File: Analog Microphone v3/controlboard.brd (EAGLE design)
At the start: 66 x 68.2 mm, 30 parts, among them J2 USB_A_SMT_FEMALE, Q1 12MHz

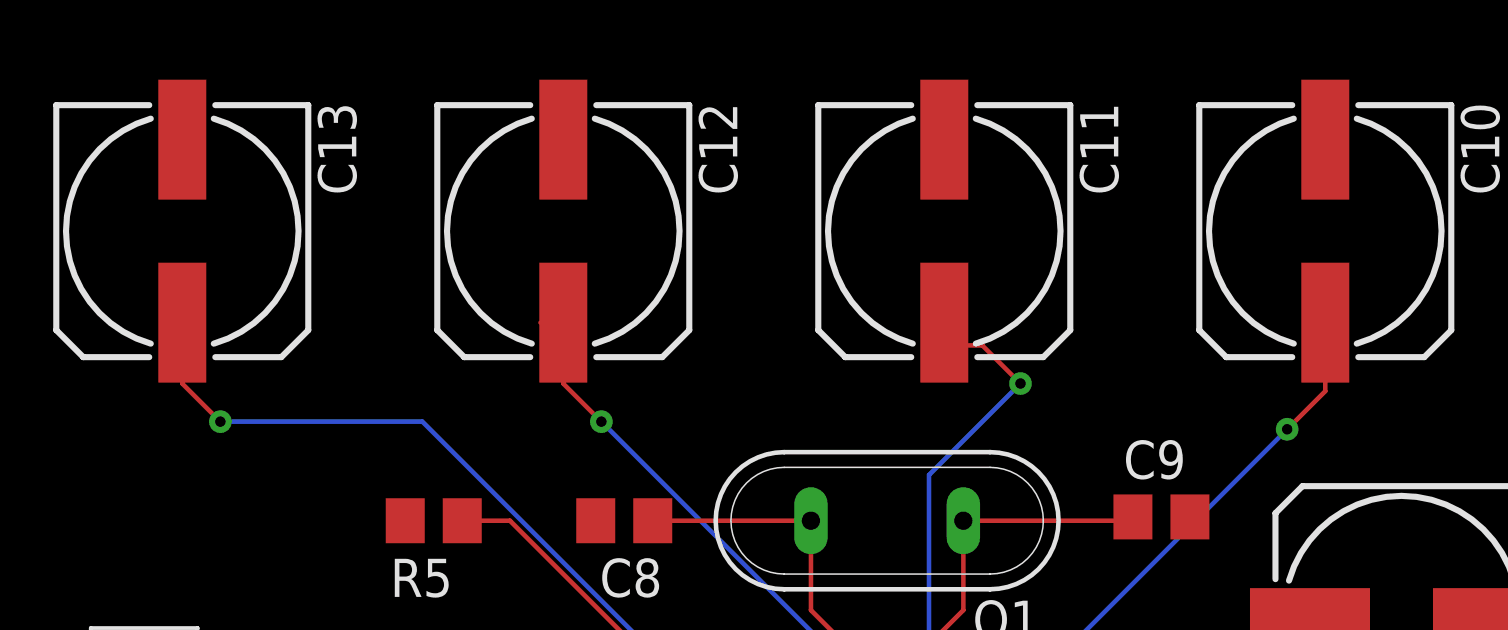
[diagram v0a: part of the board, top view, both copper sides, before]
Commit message: Update Analog Microphone v3/controlboard.brd
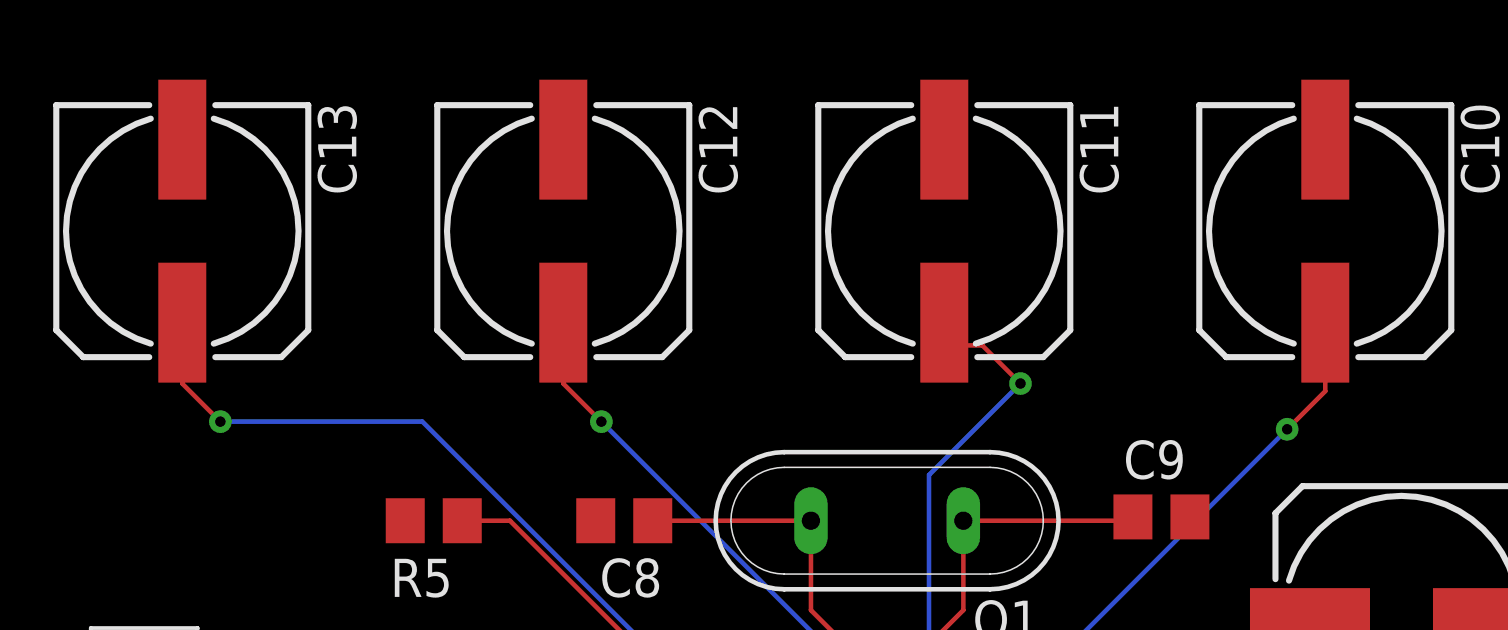
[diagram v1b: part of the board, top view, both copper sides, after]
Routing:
- net N$8: track 20.7 -> 20.0 mm
- net N$7: track 21.8 -> 21.3 mm
- net N$4: track 19.9 -> 19.4 mm
- net N$11: track 56.6 -> 56.1 mm
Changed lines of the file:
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@@
 <wire x1="35.9156" y1="42.2656" x2="36.322" y2="42.672" width="0.1524" layer="1"/>
 <via x="36.322" y="42.672" extent="1-16" drill="0.35"/>
-<wire x1="36.83" y1="57.15" x2="36.83" y2="56.64" width="0.1524" layer="1"/>
 <wire x1="36.322" y1="42.672" x2="36.322" y2="51.562" width="0.1524" layer="16"/>
 <wire x1="36.322" y1="51.562" x2="39.37" y2="54.61" width="0.1524" layer="16"/>
@@
 <via x="37.846" y="42.672" extent="1-16" drill="0.35"/>
 <wire x1="37.846" y1="42.672" x2="48.26" y2="53.086" width="0.1524" layer="16"/>
-<wire x1="49.53" y1="57.15" x2="49.53" y2="56.64" width="0.1524" layer="1"/>
 <via x="48.26" y="53.086" extent="1-16" drill="0.35"/>
 <wire x1="48.26" y1="53.086" x2="49.53" y2="54.356" width="0.1524" layer="1"/>
@@
 <via x="32.639" y="43.561" extent="1-16" drill="0.35"/>
 <wire x1="32.639" y1="43.561" x2="32.639" y2="46.101" width="0.1524" layer="16"/>
-<wire x1="24.13" y1="56.64" x2="23.37" y2="56.64" width="0.1524" layer="1"/>
 <wire x1="32.639" y1="46.101" x2="25.4" y2="53.34" width="0.1524" layer="16"/>
 <via x="25.4" y="53.34" extent="1-16" drill="0.35"/>
@@
 <wire x1="30.7086" y1="42.0624" x2="29.972" y2="42.799" width="0.1524" layer="1"/>
 <via x="29.972" y="42.799" extent="1-16" drill="0.35"/>
-<wire x1="11.43" y1="57.15" x2="11.43" y2="56.64" width="0.1524" layer="1"/>
 <wire x1="29.972" y1="42.799" x2="19.431" y2="53.34" width="0.1524" layer="16"/>
 <wire x1="19.431" y1="53.34" x2="12.7" y2="53.34" width="0.1524" layer="16"/>

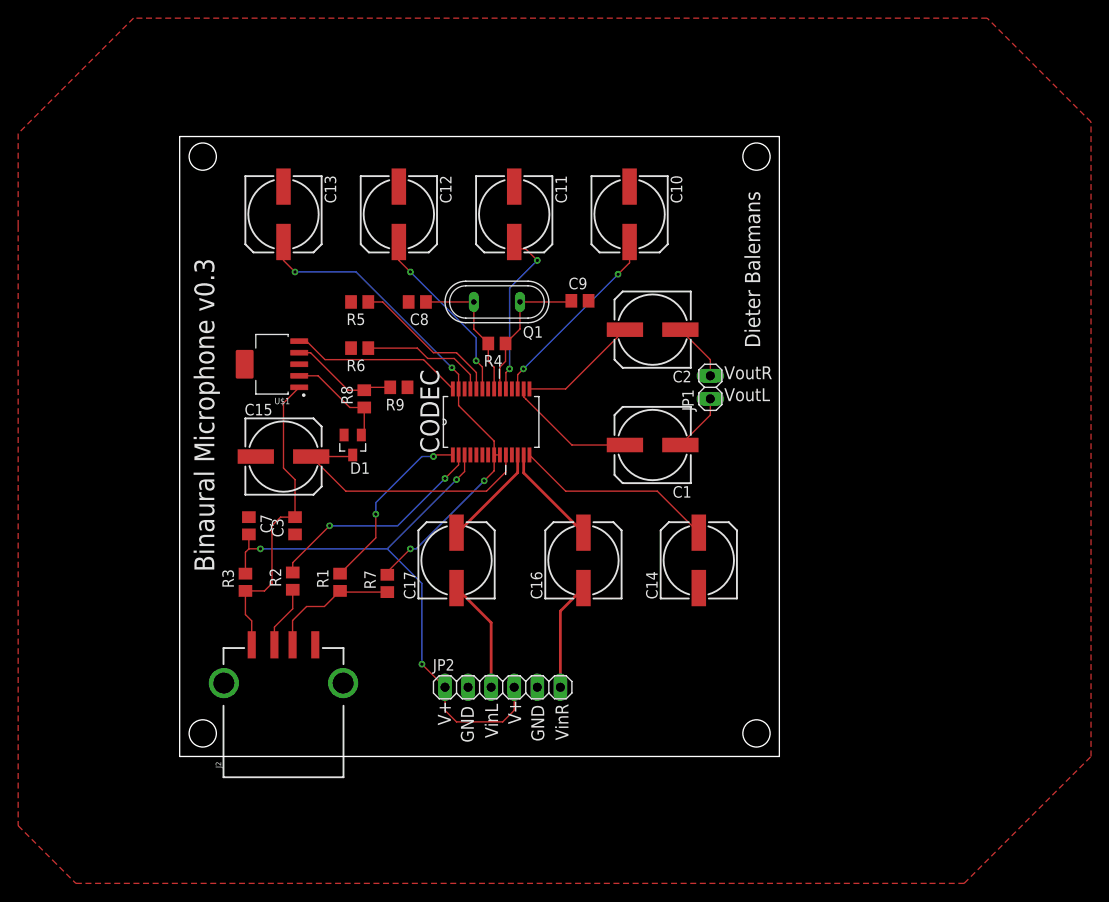
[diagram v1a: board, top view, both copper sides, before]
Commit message: Added bottom ground plane + usb test headers
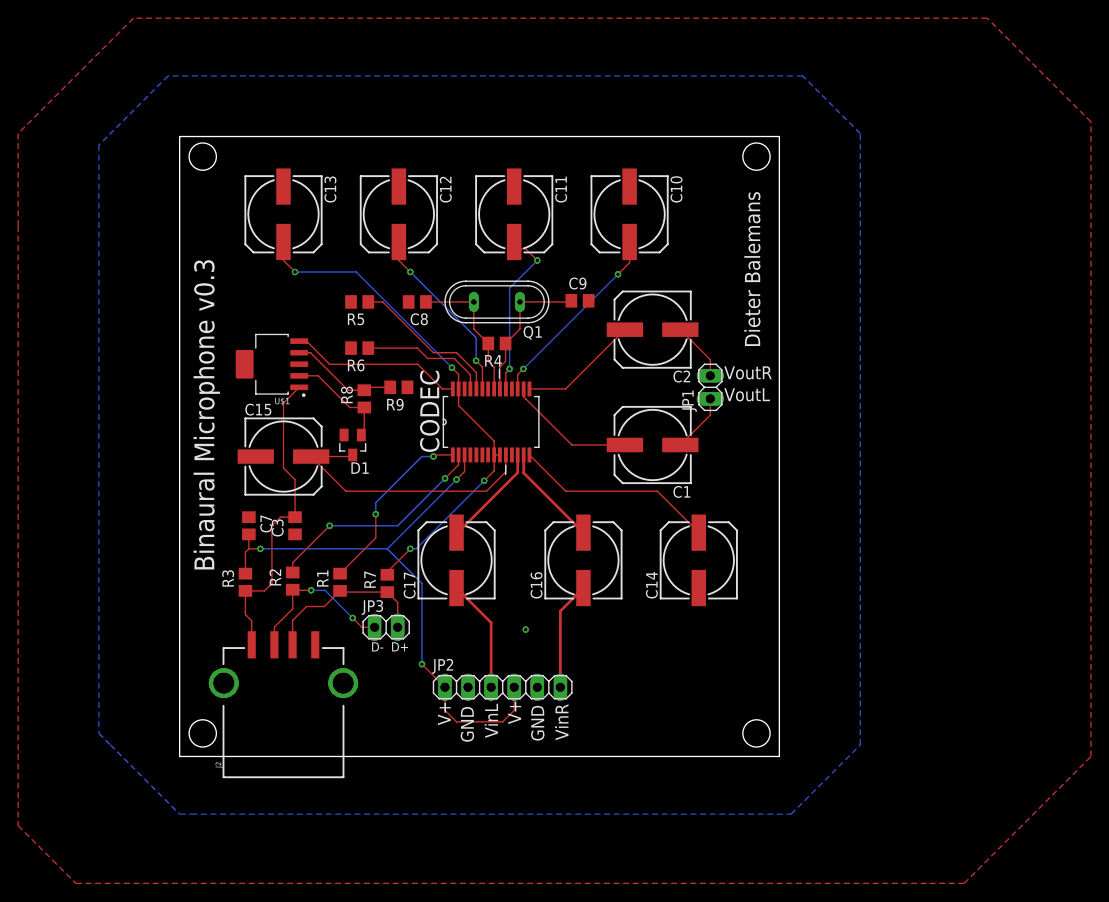
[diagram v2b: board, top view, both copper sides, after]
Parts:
- added JP3: (no value), pinhead:1X02
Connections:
- net D+: now also JP3.2
- net D-: now also JP3.1
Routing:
- net D-: track 6.90 -> 17.6 mm, vias 0 -> 2
- net D+: track 14.6 -> 18.9 mm
- added copper zone on layer 16, net GND
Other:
- board text added: "D+"
- board text added: "D-"
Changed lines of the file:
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@@
 <text x="59.944" y="41.529" size="1.4224" layer="25">VoutR</text>
 <text x="59.944" y="39.116" size="1.4224" layer="25">VoutL</text>
+<text x="25.273" y="12.573" size="1.016" layer="25" rot="R180">D+</text>
+<text x="22.479" y="12.573" size="1.016" layer="25" rot="R180">D-</text>
 </plain>
 <attributes>
@@
 <attribute name="VALUE" x="12.16" y="47.68" size="0.7" layer="27" rot="R180"/>
 </element>
+<element name="JP3" library="pinhead" library_urn="urn:adsk.eagle:library:325" package="1X02" package3d_urn="urn:adsk.eagle:package:22435/2" value="" x="22.733" y="14.224" smashed="yes">
+<attribute name="NAME" x="20.1168" y="15.9258" size="1.27" layer="25" ratio="10"/>
+<attribute name="VALUE" x="20.193" y="11.049" size="1.27" layer="27"/>
+</element>
 </elements>
 <signals>
@@
 <wire x1="12.43" y1="14.97" x2="12.43" y2="12.292" width="0.1524" layer="1"/>
 <wire x1="22.86" y1="18.1" x2="17.526" y2="18.1" width="0.1524" layer="1"/>
+<contactref element="JP3" pad="2"/>
+<wire x1="24.003" y1="14.224" x2="24.003" y2="16.957" width="0.1524" layer="1"/>
+<wire x1="24.003" y1="16.957" x2="22.86" y2="18.1" width="0.1524" layer="1"/>
 </signal>
 <signal name="D-">
@@
 <wire x1="10.43" y1="14.24" x2="10.43" y2="12.292" width="0.1524" layer="1"/>
 <wire x1="12.446" y1="16.256" x2="10.43" y2="14.24" width="0.1524" layer="1"/>
+<contactref element="JP3" pad="1"/>
+<wire x1="21.463" y1="14.224" x2="20.066" y2="14.224" width="0.1524" layer="1"/>
+<wire x1="20.066" y1="14.224" x2="19.05" y2="15.24" width="0.1524" layer="1"/>
+<via x="19.05" y="15.24" extent="1-16" drill="0.35"/>
+<wire x1="19.05" y1="15.24" x2="16.002" y2="18.288" width="0.1524" layer="16"/>
+<wire x1="16.002" y1="18.288" x2="14.478" y2="18.288" width="0.1524" layer="16"/>
+<via x="14.478" y="18.288" extent="1-16" drill="0.35"/>
+<wire x1="14.478" y1="18.288" x2="12.512" y2="18.288" width="0.1524" layer="1"/>
+<wire x1="12.512" y1="18.288" x2="12.446" y2="18.354" width="0.1524" layer="1"/>
 </signal>
 <signal name="GND">
@@
 <vertex x="-17.78" y="68.58"/>
 </polygon>
+<polygon width="0.1524" layer="16">
+<vertex x="-7.62" y="1.27"/>
+<vertex x="0" y="-6.35"/>
+<vertex x="1.27" y="-6.35"/>
+<vertex x="67.31" y="-6.35"/>
+<vertex x="74.93" y="1.27"/>
+<vertex x="74.93" y="68.58"/>
+<vertex x="68.58" y="74.93"/>
+<vertex x="-1.27" y="74.93"/>
+<vertex x="-8.89" y="67.31"/>
+<vertex x="-8.89" y="2.54"/>
+</polygon>
+<via x="38.1" y="13.97" extent="1-16" drill="0.35" shape="octagon"/>
 </signal>
 <signal name="VBUS">
@@
 <contactref element="CODEC" pad="28"/>
 <contactref element="U$1" pad="5"/>
-<wire x1="30.0736" y1="40.4622" x2="26.8478" y2="43.688" width="0.1524" layer="1"/>
-<wire x1="16.002" y1="43.688" x2="13.97" y2="45.72" width="0.1524" layer="1"/>
+<wire x1="30.0736" y1="40.4622" x2="28.9306" y2="40.4622" width="0.1524" layer="1"/>
+<wire x1="28.9306" y1="40.4622" x2="26.2128" y2="43.18" width="0.1524" layer="1"/>
+<wire x1="16.51" y1="43.18" x2="13.97" y2="45.72" width="0.1524" layer="1"/>
 <wire x1="13.97" y1="45.72" x2="13.165" y2="45.72" width="0.1524" layer="1"/>
-<wire x1="26.8478" y1="43.688" x2="16.002" y2="43.688" width="0.1524" layer="1"/>
+<wire x1="26.2128" y1="43.18" x2="16.51" y2="43.18" width="0.1524" layer="1"/>
 </signal>
 <signal name="N$13">
